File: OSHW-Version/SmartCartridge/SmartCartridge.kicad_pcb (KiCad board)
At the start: 2 copper layers, 280.5 x 39.3 mm, 6 parts, among them SW1 SW_Push

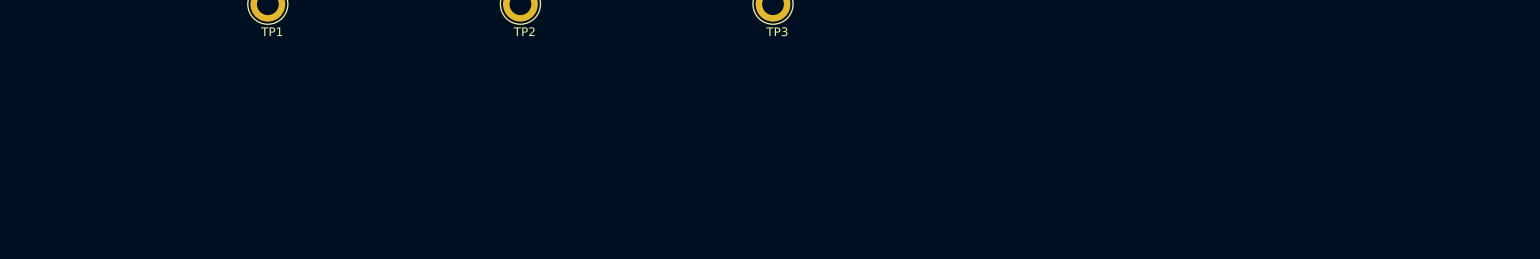
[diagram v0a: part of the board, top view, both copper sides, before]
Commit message: readme refacto, add datasheet, add led display, progress smartcartridge
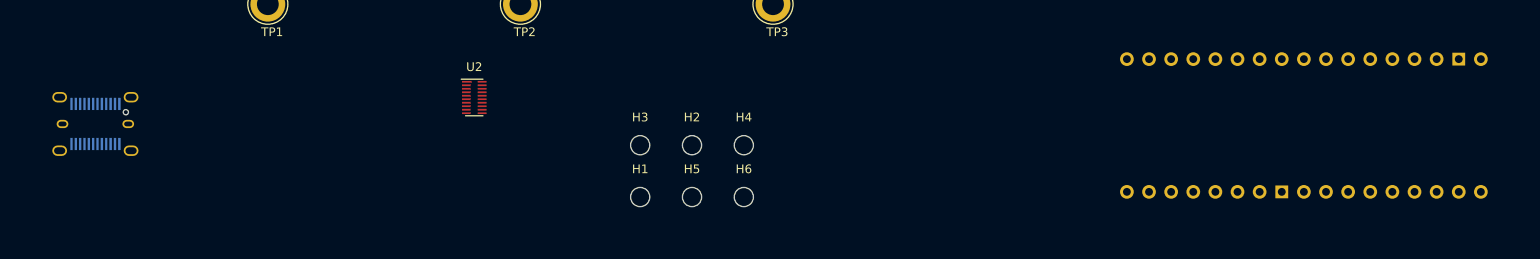
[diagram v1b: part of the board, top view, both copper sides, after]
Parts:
- added H1: MountingHole, MountingHole:MountingHole_2.2mm_M2, F.Cu at (158.8, 104.1)
- added H2: MountingHole, MountingHole:MountingHole_2.2mm_M2, F.Cu at (164.7, 98.2)
- added H3: MountingHole, MountingHole:MountingHole_2.2mm_M2, F.Cu at (158.8, 98.2)
- added H4: MountingHole, MountingHole:MountingHole_2.2mm_M2, F.Cu at (170.7, 98.2)
- added H5: MountingHole, MountingHole:MountingHole_2.2mm_M2, F.Cu at (164.7, 104.1)
- added H6: MountingHole, MountingHole:MountingHole_2.2mm_M2, F.Cu at (170.7, 104.1)
- added J5: USB_C_Receptacle, Connector_USB:USB_C_Receptacle_JAE_DX07S024WJ1R350, B.Cu at (96.2, 95.8)
- added U1: ProS3, footprint:ProS3_TH, B.Cu at (234.9, 95.9)
- added U2: TXB0108DQSR, Package_SON:USON-20_2x4mm_P0.4mm, F.Cu at (139.7, 92.7)
